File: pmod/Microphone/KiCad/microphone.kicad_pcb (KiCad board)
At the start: 2 copper layers, 43.5 x 34 mm, 16 parts, among them IC1 MAX4466EXK+T, J1 Conn_01x06_Pin

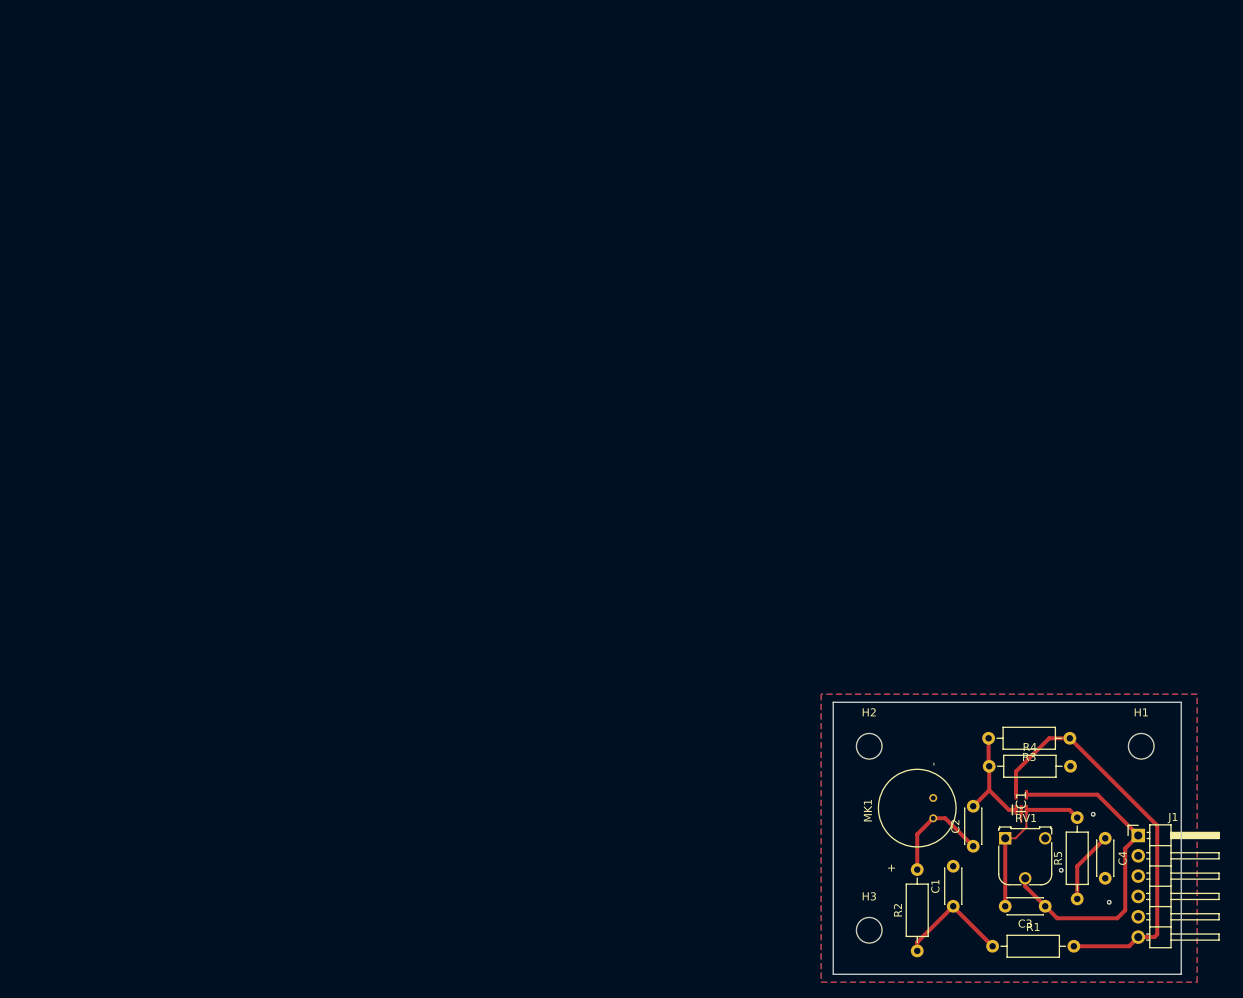
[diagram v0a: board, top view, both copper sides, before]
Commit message: Replace MAX4466 with LM321U
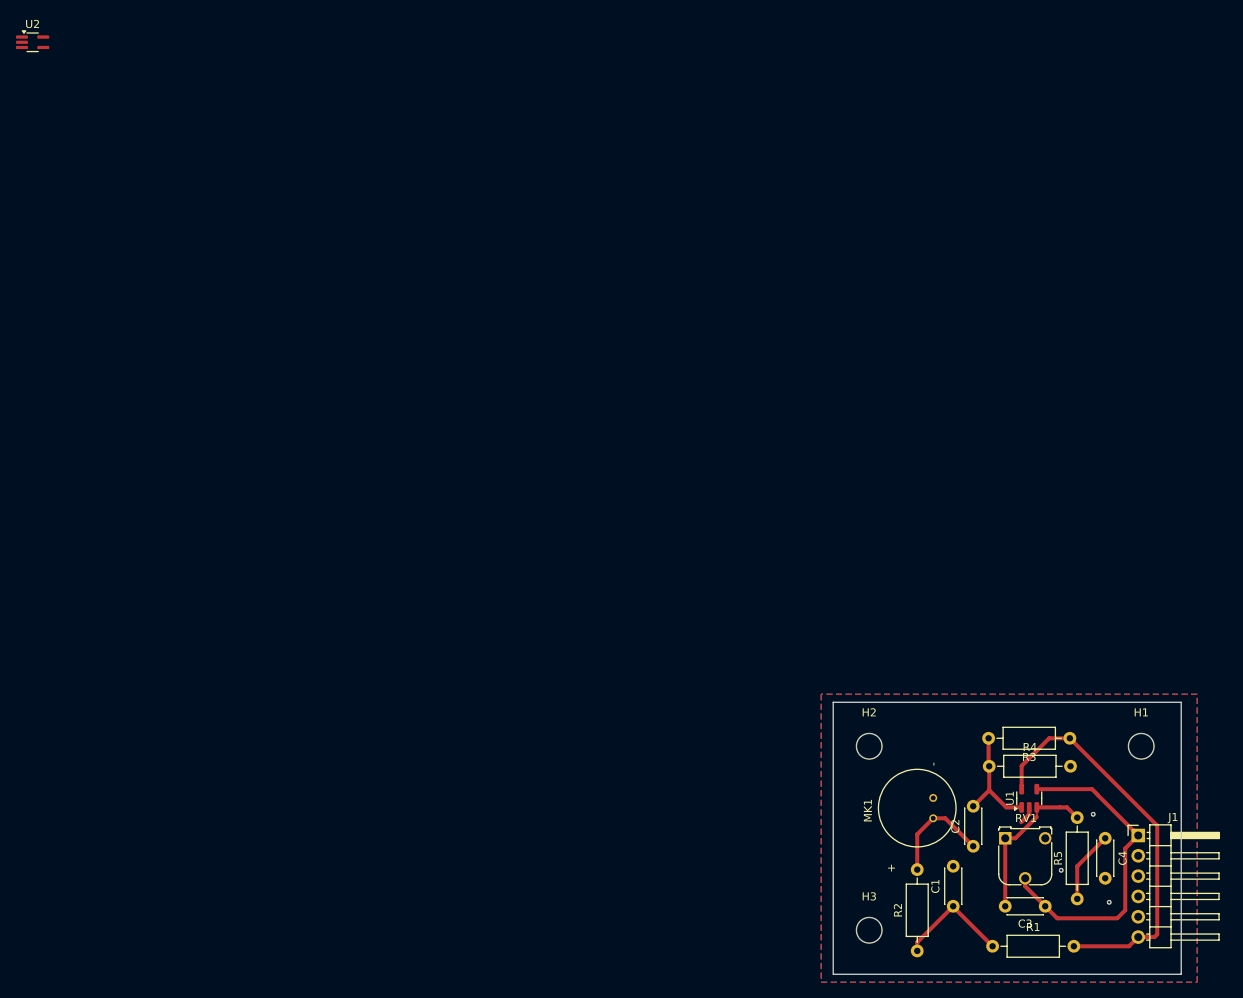
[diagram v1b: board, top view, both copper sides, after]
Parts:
- removed IC1: MAX4466EXK+T, MAX4466:SOT65P210X110-5N
- added U1: LMV321, Package_TO_SOT_SMD:SOT-23-5, F.Cu at (127.0, 96.0)
- added U2: LMV321, Package_TO_SOT_SMD:SOT-353_SC-70-5_Handsoldering, F.Cu at (2.42, 1.50)
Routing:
- net Net-(J1-Pin_1): track 42.0 -> 41.0 mm
- net +3V3: track 51.4 -> 50.4 mm
- net GND: track 2.23 -> 2.96 mm
- net Net-(U1-+): track 13.7 -> 14.3 mm

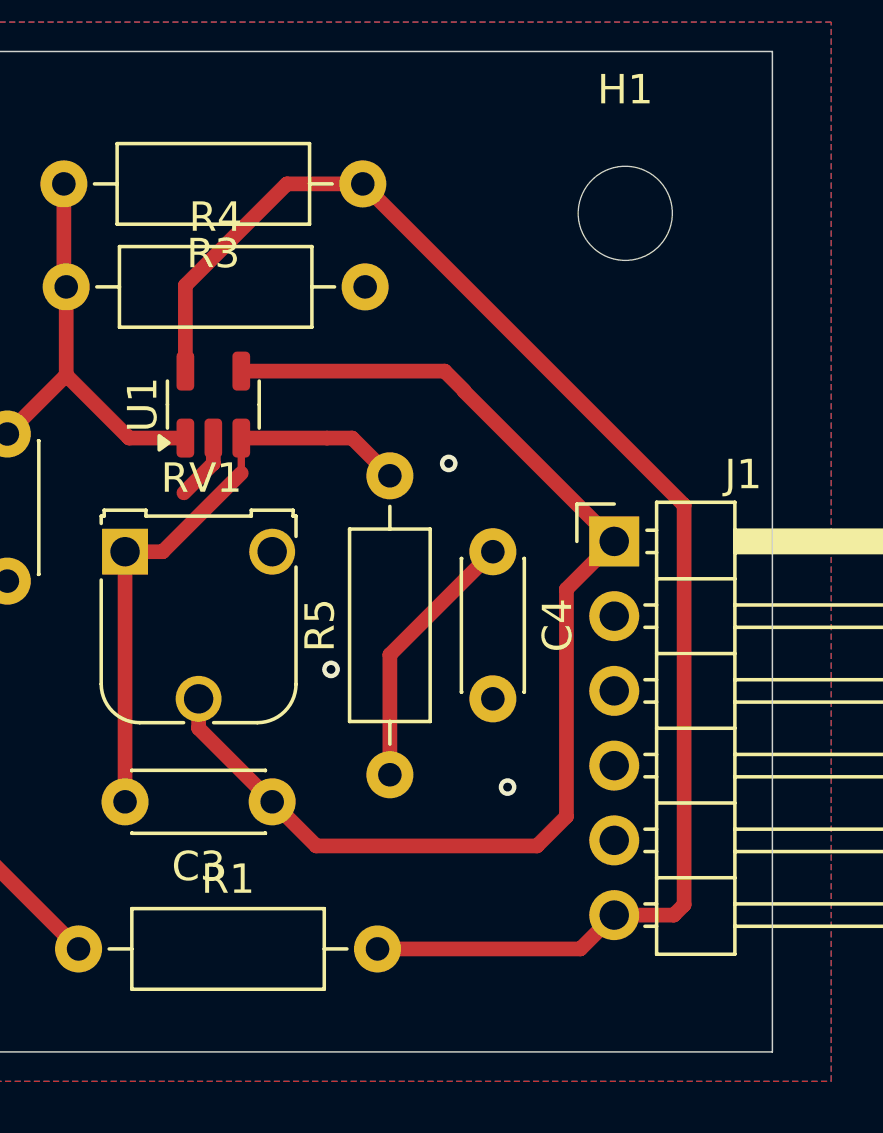
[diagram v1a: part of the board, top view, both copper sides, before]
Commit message: Flip P-MOD connector to align with OG PMOD devices and add Mouser hyperlink for the opamp
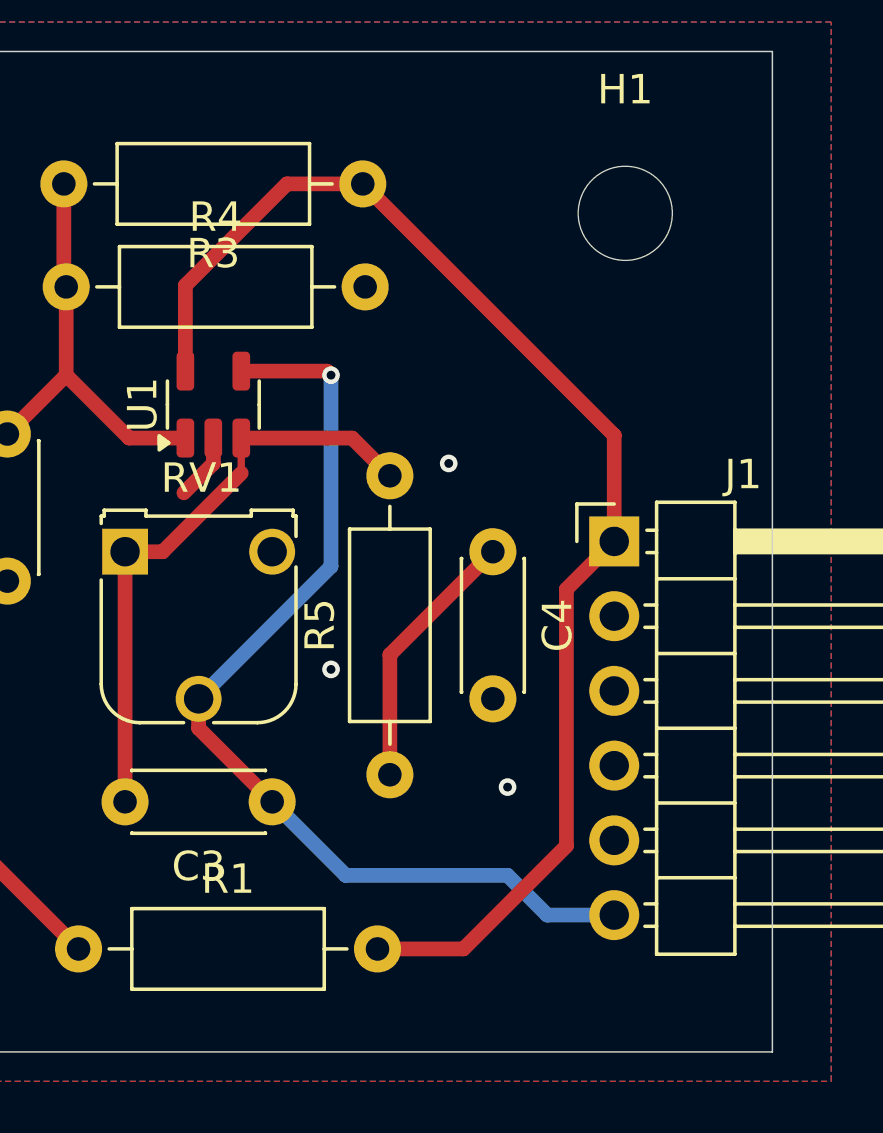
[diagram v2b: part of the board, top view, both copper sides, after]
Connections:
- C3 pad 1: Net-(J1-Pin_1) -> Net-(J1-Pin_6)
- J1 pad 1: Net-(J1-Pin_1) -> +3V3
- J1 pad 2: unconnected-(J1-Pin_2-Pad2) -> GND
- J1 pad 5: GND -> unconnected-(J1-Pin_5-Pad5)
- J1 pad 6: +3V3 -> Net-(J1-Pin_6)
- RV1 pad 2: Net-(J1-Pin_1) -> Net-(J1-Pin_6)
- U1 pad 4: Net-(J1-Pin_1) -> Net-(J1-Pin_6)
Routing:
- net Net-(J1-Pin_1): track 41.0 -> 0.00 mm
- net Net-(J1-Pin_6): track 0.00 -> 33.7 mm, vias 0 -> 1
- net +3V3: track 50.4 -> 45.2 mm
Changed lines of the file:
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@@
 	(net 5 "+3V3")
 	(net 6 "unconnected-(RV1-Pad3)")
-	(net 7 "unconnected-(J1-Pin_2-Pad2)")
+	(net 7 "Net-(J1-Pin_6)")
 	(net 8 "unconnected-(J1-Pin_4-Pad4)")
 	(net 9 "unconnected-(J1-Pin_3-Pad3)")
 	(net 10 "Net-(U1-+)")
-	(net 11 "Net-(J1-Pin_1)")
+	(net 11 "unconnected-(J1-Pin_5-Pad5)")
 	(net 12 "Net-(U1--)")
 	(net 13 "unconnected-(U2-+-Pad1)")
@@
 			)
 			(remove_unused_layers no)
-			(net 11 "Net-(J1-Pin_1)")
+			(net 7 "Net-(J1-Pin_6)")
 			(pinfunction "2")
 			(pintype "passive")
@@
 			(layers "F.Cu" "F.Paste" "F.Mask")
 			(roundrect_rratio 0.25)
-			(net 11 "Net-(J1-Pin_1)")
+			(net 7 "Net-(J1-Pin_6)")
 			(pintype "output")
 		)
@@
 			)
 			(remove_unused_layers no)
-			(net 11 "Net-(J1-Pin_1)")
+			(net 7 "Net-(J1-Pin_6)")
 			(pintype "passive")
 		)
@@
 			)
 			(remove_unused_layers no)
-			(net 11 "Net-(J1-Pin_1)")
+			(net 5 "+3V3")
 			(pinfunction "Pin_1")
 			(pintype "passive")
@@
 			)
 			(remove_unused_layers no)
-			(net 7 "unconnected-(J1-Pin_2-Pad2)")
+			(net 1 "GND")
 			(pinfunction "Pin_2")
 			(pintype "passive")
@@
 			)
 			(remove_unused_layers no)
-			(net 1 "GND")
+			(net 11 "unconnected-(J1-Pin_5-Pad5)")
 			(pinfunction "Pin_5")
 			(pintype "passive")
@@
 			)
 			(remove_unused_layers no)
-			(net 5 "+3V3")
+			(net 7 "Net-(J1-Pin_6)")
 			(pinfunction "Pin_6")
 			(pintype "passive")
@@
 	)
 	(segment
-		(start 129.5 88.5)
-		(end 132.08 88.5)
+		(start 132.08 88.5)
+		(end 140.625 97.045)
 		(width 0.5)
 		(layer "F.Cu")
@@
 	)
 	(segment
-		(start 139.475 114.5)
-		(end 132.58 114.5)
+		(start 140.625 97.045)
+		(end 140.625 100.65)
 		(width 0.5)
 		(layer "F.Cu")
@@
 	)
 	(segment
-		(start 143 113)
-		(end 143 99.42)
-		(width 0.5)
+		(start 140.625 100.65)
+		(end 140.35 100.65)
+		(width 0.2)
 		(layer "F.Cu")
 		(net 5)
 	)
 	(segment
-		(start 142.65 113.35)
-		(end 143 113)
+		(start 139 102.275)
+		(end 140.625 100.65)
 		(width 0.5)
 		(layer "F.Cu")
@@
 	)
 	(segment
-		(start 126.05 91.95)
-		(end 126.05 94.8625)
+		(start 129.5 88.5)
+		(end 132.08 88.5)
 		(width 0.5)
 		(layer "F.Cu")
@@
 	)
 	(segment
-		(start 140.625 113.35)
-		(end 139.475 114.5)
+		(start 135.5 114.5)
+		(end 139 111)
 		(width 0.5)
 		(layer "F.Cu")
@@
 	)
 	(segment
-		(start 140.625 113.35)
-		(end 142.65 113.35)
+		(start 139 111)
+		(end 139 102.275)
 		(width 0.5)
 		(layer "F.Cu")
@@
 	)
 	(segment
-		(start 129.5 88.5)
-		(end 126.05 91.95)
+		(start 126.05 91.95)
+		(end 126.05 94.8625)
 		(width 0.5)
 		(layer "F.Cu")
@@
 	)
 	(segment
-		(start 143 99.42)
-		(end 132.08 88.5)
+		(start 129.5 88.5)
+		(end 126.05 91.95)
 		(width 0.5)
 		(layer "F.Cu")
@@
 	)
 	(segment
-		(start 122 95)
-		(end 120 97)
+		(start 132.58 114.5)
+		(end 135.5 114.5)
 		(width 0.5)
 		(layer "F.Cu")
-		(net 10)
+		(net 5)
 	)
 	(segment
-		(start 121.92 88.5)
-		(end 121.92 91.92)
+		(start 131 95)
+		(end 130.8625 94.8625)
 		(width 0.5)
 		(layer "F.Cu")
-		(net 10)
+		(net 7)
 	)
 	(segment
-		(start 124.1375 97.1375)
-		(end 126.05 97.1375)
+		(start 130.8625 94.8625)
+		(end 127.95 94.8625)
 		(width 0.5)
 		(layer "F.Cu")
-		(net 10)
-	)
-	(segment
-		(start 121.92 91.92)
-		(end 122 92)
-		(width 0.2)
-		(layer "F.Cu")
-		(net 10)
+		(net 7)
 	)
 	(segment
-		(start 122 95)
-		(end 124.1375 97.1375)
+		(start 126.5 107)
+		(end 126.5 106)
 		(width 0.5)
 		(layer "F.Cu")
-		(net 10)
+		(net 7)
 	)
 	(segment
-		(start 122 92)
-		(end 122 95)
+		(start 129 109.5)
+		(end 126.5 107)
 		(width 0.5)
 		(layer "F.Cu")
-		(net 10)
+		(net 7)
+	)
+	(via
+		(at 131 95)
+		(size 0.6)
+		(drill 0.3)
+		(layers "F.Cu" "B.Cu")
+		(net 7)
 	)
 	(segment
-		(start 130.5 111)
-		(end 138 111)
+		(start 131.5 112)
+		(end 137 112)
 		(width 0.5)
-		(layer "F.Cu")
-		(net 11)
+		(layer "B.Cu")
+		(net 7)
 	)
 	(segment
-		(start 135.525 95.55)
-		(end 140.625 100.65)
+		(start 138.35 113.35)
+		(end 140.625 113.35)
 		(width 0.5)
-		(layer "F.Cu")
-		(net 11)
+		(layer "B.Cu")
+		(net 7)
 	)
 	(segment
-		(start 129 109.5)
-		(end 130.5 111)
+		(start 137 112)
+		(end 138.35 113.35)
 		(width 0.5)
-		(layer "F.Cu")
-		(net 11)
+		(layer "B.Cu")
+		(net 7)
 	)
 	(segment
-		(start 138 111)
-		(end 139 110)
+		(start 131 101.5)
+		(end 131 95)
 		(width 0.5)
-		(layer "F.Cu")
-		(net 11)
+		(layer "B.Cu")
+		(net 7)
 	)
 	(segment
-		(start 140.625 100.65)
-		(end 140.35 100.65)
-		(width 0.2)
-		(layer "F.Cu")
-		(net 11)
+		(start 126.5 106)
+		(end 131 101.5)
+		(width 0.5)
+		(layer "B.Cu")
+		(net 7)
 	)
 	(segment
-		(start 135.525 95.525)
-		(end 135.525 95.55)
-		(width 0.2)
-		(layer "F.Cu")
-		(net 11)
+		(start 129 109.5)
+		(end 131.5 112)
+		(width 0.5)
+		(layer "B.Cu")
+		(net 7)
 	)
 	(segment
-		(start 126.5 107)
-		(end 126.5 106)
+		(start 122 95)
+		(end 120 97)
 		(width 0.5)
 		(layer "F.Cu")
-		(net 11)
+		(net 10)
 	)
 	(segment
-		(start 139 110)
-		(end 139 102.275)
+		(start 121.92 88.5)
+		(end 121.92 91.92)
 		(width 0.5)
 		(layer "F.Cu")
-		(net 11)
+		(net 10)
 	)
 	(segment
-		(start 134.8625 94.8625)
-		(end 135.525 95.525)
+		(start 124.1375 97.1375)
+		(end 126.05 97.1375)
 		(width 0.5)
 		(layer "F.Cu")
-		(net 11)
+		(net 10)
 	)
 	(segment
-		(start 127.95 94.8625)
-		(end 134.8625 94.8625)
-		(width 0.5)
+		(start 121.92 91.92)
+		(end 122 92)
+		(width 0.2)
 		(layer "F.Cu")
-		(net 11)
+		(net 10)
 	)
 	(segment
-		(start 139 102.275)
-		(end 140.625 100.65)
+		(start 122 95)
+		(end 124.1375 97.1375)
 		(width 0.5)
 		(layer "F.Cu")
-		(net 11)
+		(net 10)
 	)
 	(segment
-		(start 129 109.5)
-		(end 126.5 107)
+		(start 122 92)
+		(end 122 95)
 		(width 0.5)
 		(layer "F.Cu")
-		(net 11)
+		(net 10)
 	)
 	(segment

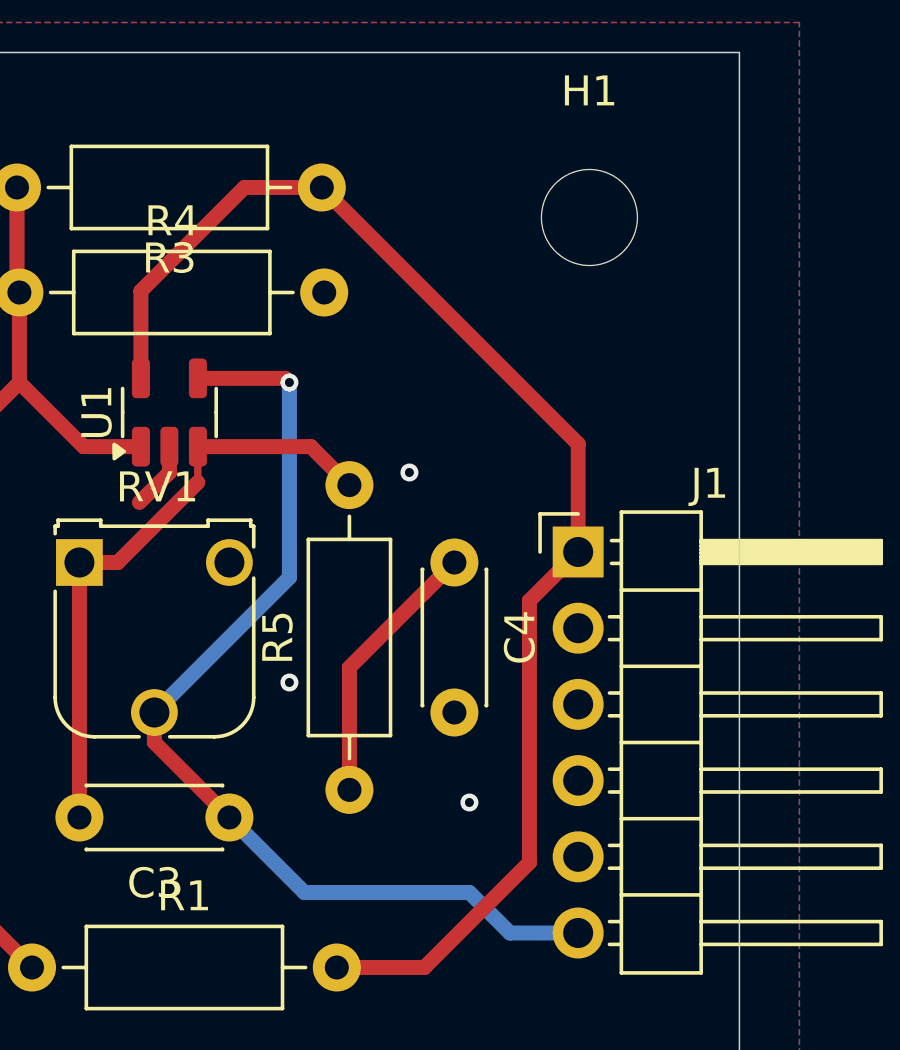
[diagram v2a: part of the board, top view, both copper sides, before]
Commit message: Add fourth hole
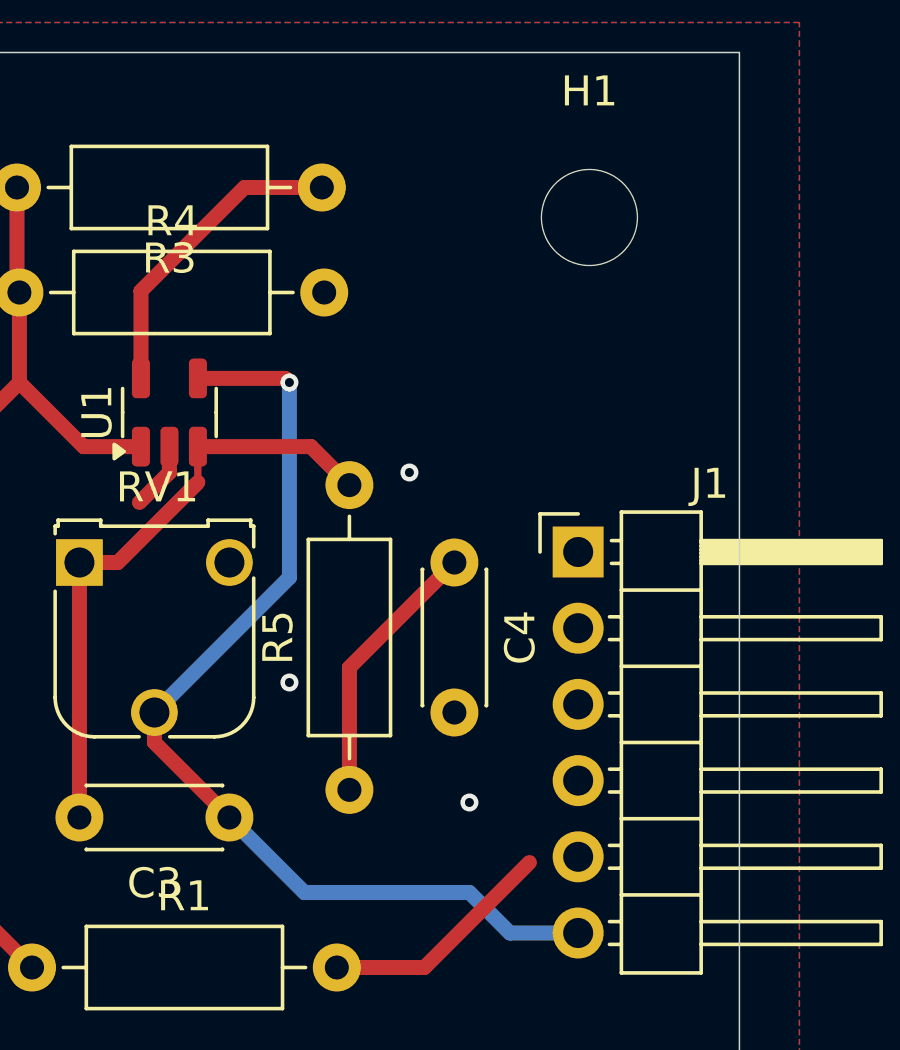
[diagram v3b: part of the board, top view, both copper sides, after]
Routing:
- net +3V3: track 45.2 -> 18.5 mm
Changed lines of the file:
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@@
-	)
-	(segment
-		(start 132.08 88.5)
-		(end 140.625 97.045)
-		(width 0.5)
-		(layer "F.Cu")
-		(net 5)
-	)
-	(segment
-		(start 140.625 97.045)
-		(end 140.625 100.65)
-		(width 0.5)
-		(layer "F.Cu")
-		(net 5)
 	)
 	(segment
@@
 		(end 140.35 100.65)
 		(width 0.2)
-		(layer "F.Cu")
-		(net 5)
-	)
-	(segment
-		(start 139 102.275)
-		(end 140.625 100.65)
-		(width 0.5)
 		(layer "F.Cu")
 		(net 5)
@@
 		(width 0.5)
 		(layer "F.Cu")
-		(net 5)
-	)
-	(segment
-		(start 139 111)
-		(end 139 102.275)
-		(width 0.5)
-		(layer "F.Cu")
